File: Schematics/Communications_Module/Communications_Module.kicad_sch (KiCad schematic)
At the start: 74 parts, among them J2 SWD_01x04_Pin, J3 Stack Male Edge Connector, J4 USB_C_Female_USB2_Small, Q1 AO3400A, SW1 SW_STM_RESET, SW2 SW_STM_BOOT_MODE, U1 RFM95W-915S2, U12 AMS1117-3.3, U2 W25Q128JVS, U4 LM66100DCKR, U5 LM66100DCKR, U6 LM66100DCKR, U7 STM32F103CBT6, U8 ACS70331EOLC, U9 ISO1042BDWVR, Y1 X322516MMB4SI

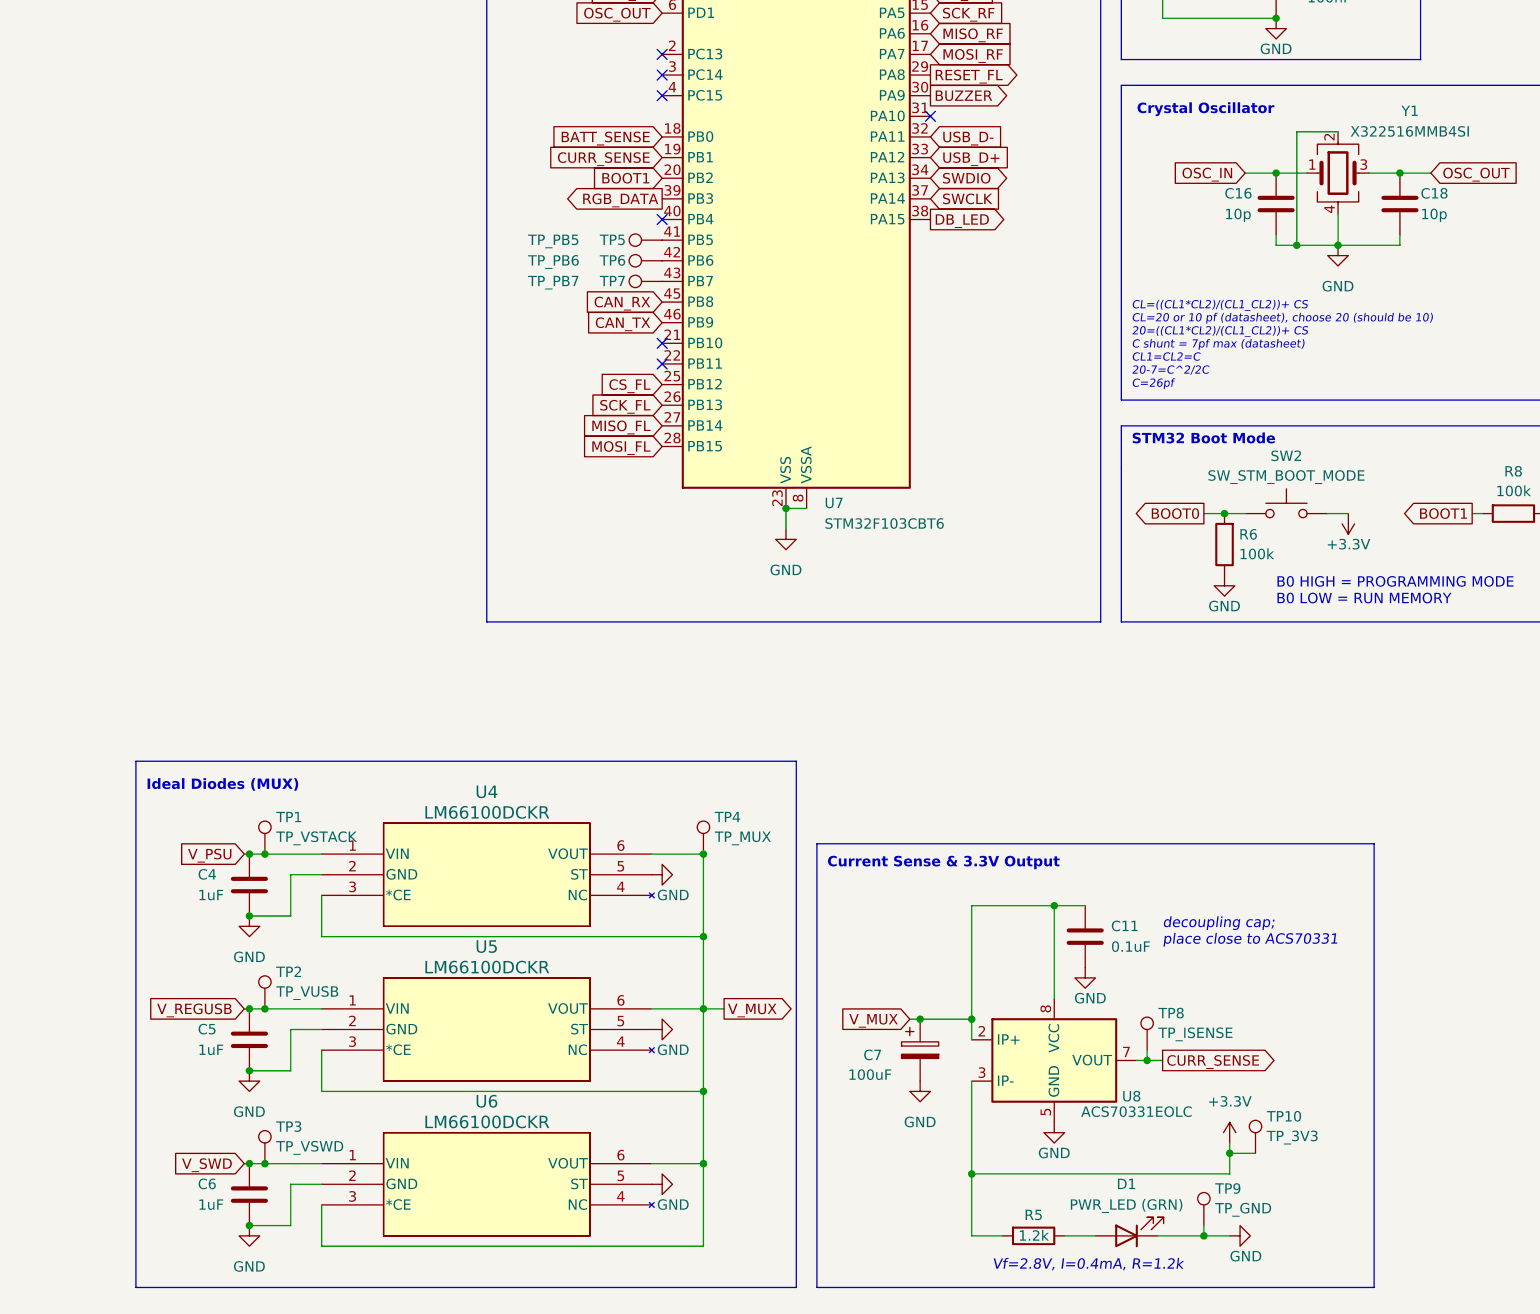
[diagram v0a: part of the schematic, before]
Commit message: Removed current sensor + reduced PWR LED brightness
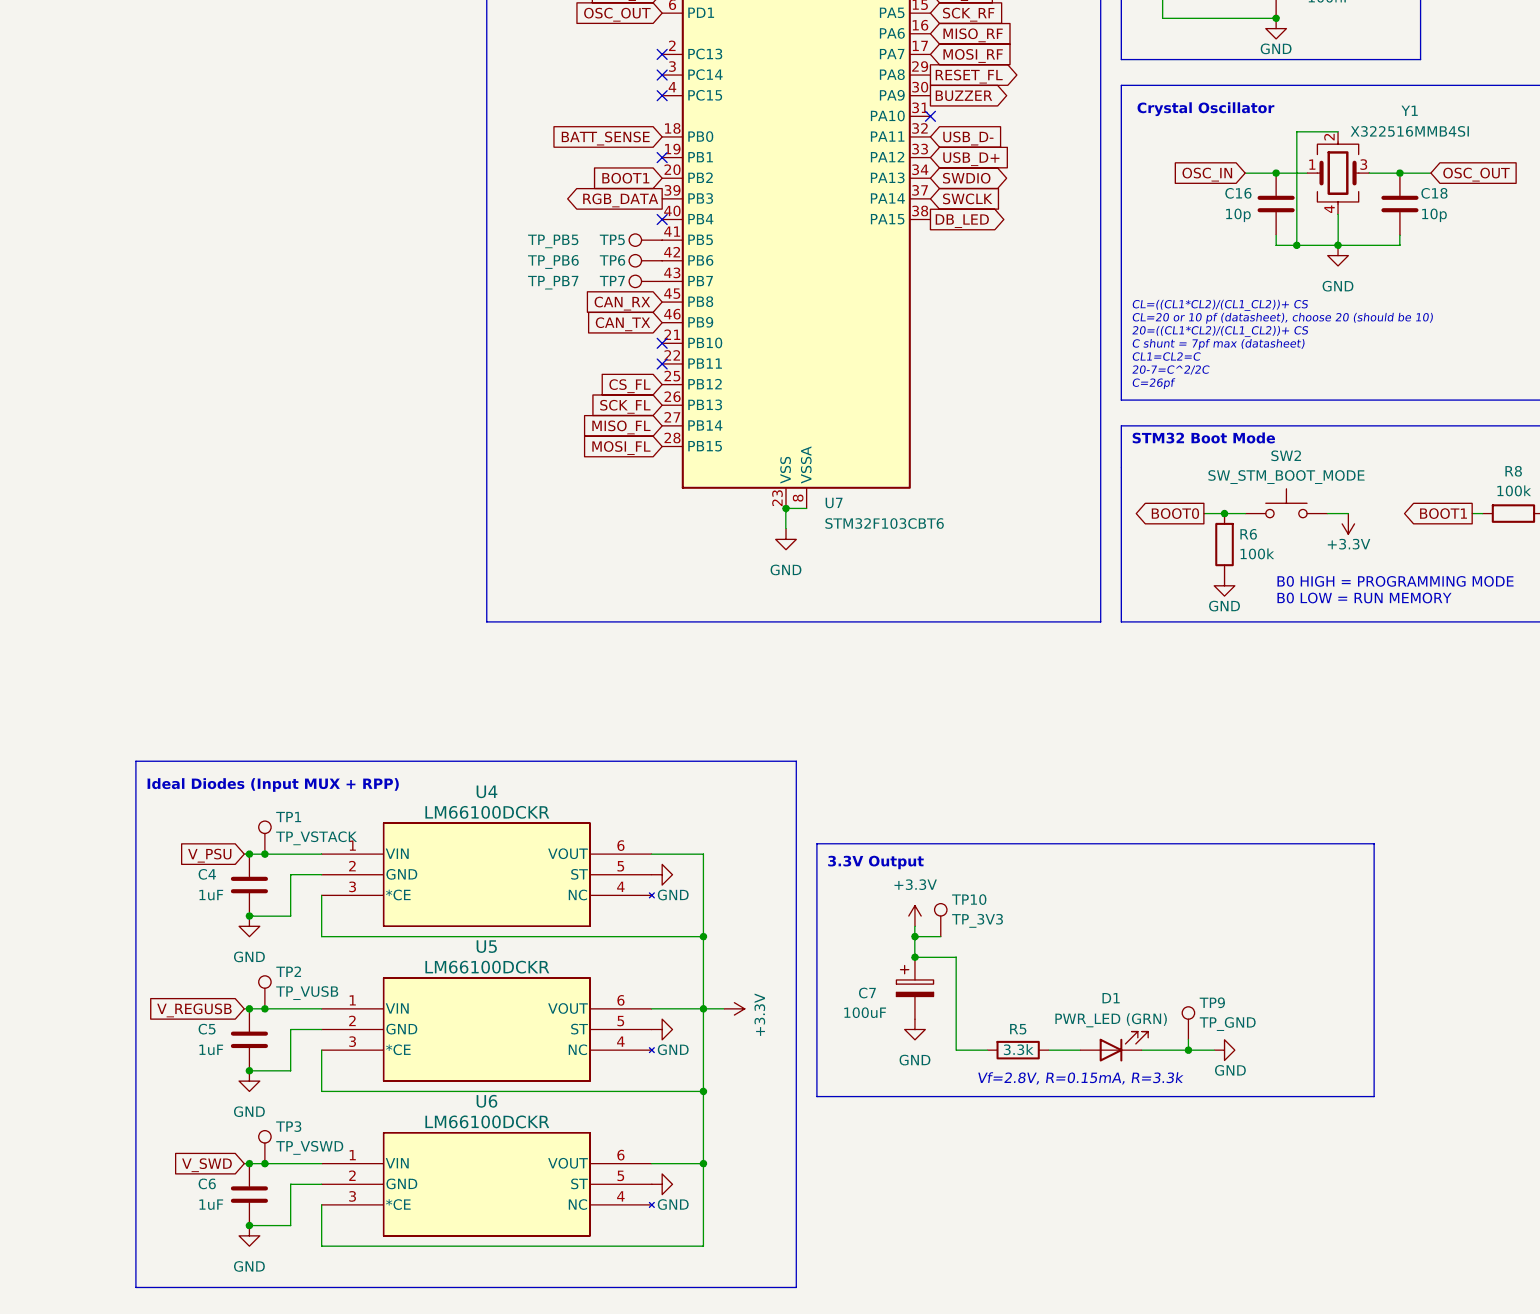
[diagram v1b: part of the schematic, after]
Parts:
- removed C11: 0.1uF, Capacitor_SMD:C_0603_1608Metric, symbol Device:C
- removed TP4: TP_MUX, TestPoint:TestPoint_Pad_1.5x1.5mm, symbol Connector:TestPoint
- removed TP8: TP_ISENSE, TestPoint:TestPoint_Pad_1.5x1.5mm, symbol Connector:TestPoint
- removed U8: ACS70331EOLC, footprints:SOIC127P600X175-8N, symbol Sensor_Current:ACS706xLC-05C
- R5: value 1.2k -> 3.3k; LCSC C22765 -> C22978
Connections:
- net V_MUX is gone; now on net +3.3V: C7.1, U4.3 (*CE), U4.6 (VOUT), U5.3 (*CE), U5.6 (VOUT), U6.3 (*CE), U6.6 (VOUT)
- net CURR_SENSE: no longer names the net of U7.19 (PB1)
- no-connect marks 18 -> 19
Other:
- note added: "3.3V Output"
- note added: "Ideal Diodes (Input MUX + RPP)"
- note added: "Vf=2.8V, R=0.15mA, R=3.3k"
- note removed: "Current Sense & 3.3V Output"
- note removed: "Ideal Diodes (MUX)"
- note removed: "Vf=2.8V, I=0.4mA, R=1.2k"
- note removed: "decoupling cap; place close to ACS70331"
- moved on the sheet: C7, D1, R5, TP10, TP9

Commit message: Changed SWD header to SMD version
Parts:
- J2: footprint SWD_Header:SWD_PinHeader_1x04_P2.54mm_Horizontal -> SWD_Header:SWD_PinHeader_1x04_P2.54mm_Horizontal_SMD
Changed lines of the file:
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@@
       (effects (font (size 1.27 1.27)) (justify right))
     )
-    (property "Footprint" "SWD_Header:SWD_PinHeader_1x04_P2.54mm_Horizontal" (at 31.75 176.53 0)
+    (property "Footprint" "SWD_Header:SWD_PinHeader_1x04_P2.54mm_Horizontal_SMD" (at 31.75 176.53 0)
       (effects (font (size 1.27 1.27)) hide)
     )

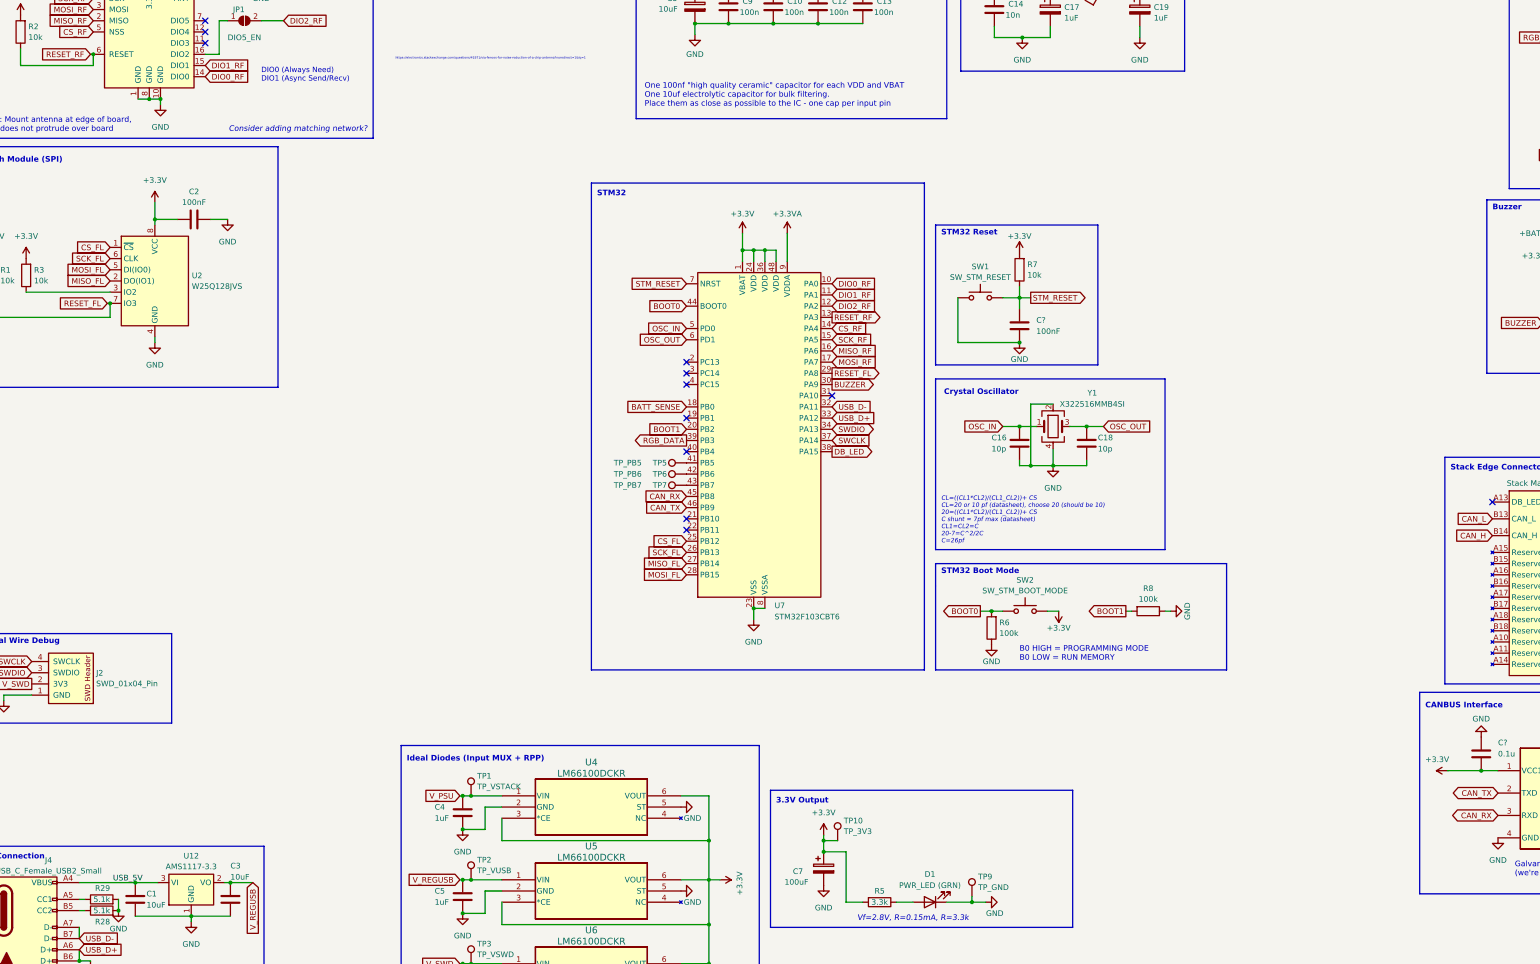
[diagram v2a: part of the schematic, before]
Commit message: Added CP2102 USB-UART bridge
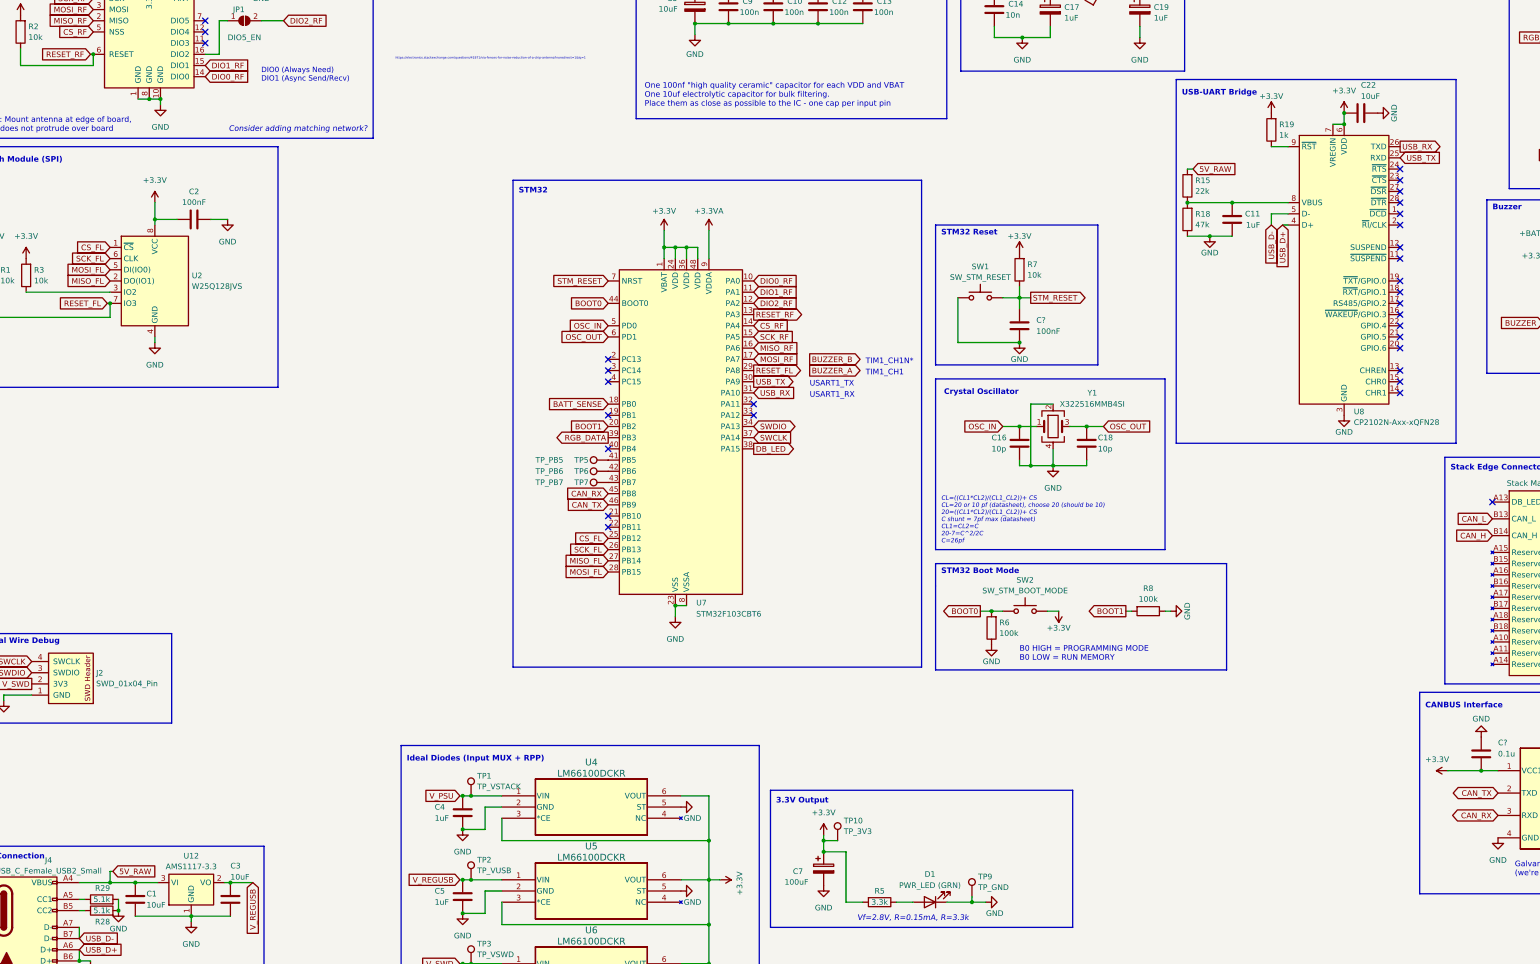
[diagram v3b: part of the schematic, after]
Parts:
- added C11: 1uF, Capacitor_SMD:C_0603_1608Metric, symbol Device:C
- added C22: 10uF, Capacitor_SMD:C_0603_1608Metric, symbol Device:C
- added R15: 22k, Resistor_SMD:R_0603_1608Metric, symbol Device:R
- added R18: 47k, Resistor_SMD:R_0603_1608Metric, symbol Device:R
- added R19: 1k, Resistor_SMD:R_0603_1608Metric, symbol Device:R
- added U8: CP2102N-Axx-xQFN28, Package_DFN_QFN:QFN-28-1EP_5x5mm_P0.5mm_EP3.35x3.35mm, symbol Interface_USB:CP2102N-Axx-xQFN28
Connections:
- net +3.3V: now also C22.2, R19.2, U8.6 (VDD), U8.7 (VREGIN)
- net BUZZER: no longer U7.30 (PA9)
- net GND: now also C11.1, C22.1, R18.1, U8.29 (GND), U8.3 (GND)
- net USB_D+: now also U8.4 (D+); no longer U7.33 (PA12)
- net USB_D-: now also U8.5 (D-); no longer U7.32 (PA11)
- net USB_RX: now reaches U7.31 (PA10)
- net USB_RX: now also U8.26 (TXD)
- net USB_5V renamed 5V_RAW
- net 5V_RAW: now also R15.2
- new net: R19.1, U8.9 (~{RST})
- new net: C11.2, R15.1, R18.2, U8.8 (VBUS)
- new net USB_TX: U7.30 (PA9), U8.25 (RXD)
- no-connect marks 19 -> 38
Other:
- note added: "TIM1_CH1"
- note added: "TIM1_CH1N*"
- note added: "USART1_RX"
- note added: "USART1_TX"
- note added: "USB-UART Bridge"
- moved on the sheet: TP5, TP6, TP7, U7
